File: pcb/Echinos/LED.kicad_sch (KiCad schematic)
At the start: 14 parts

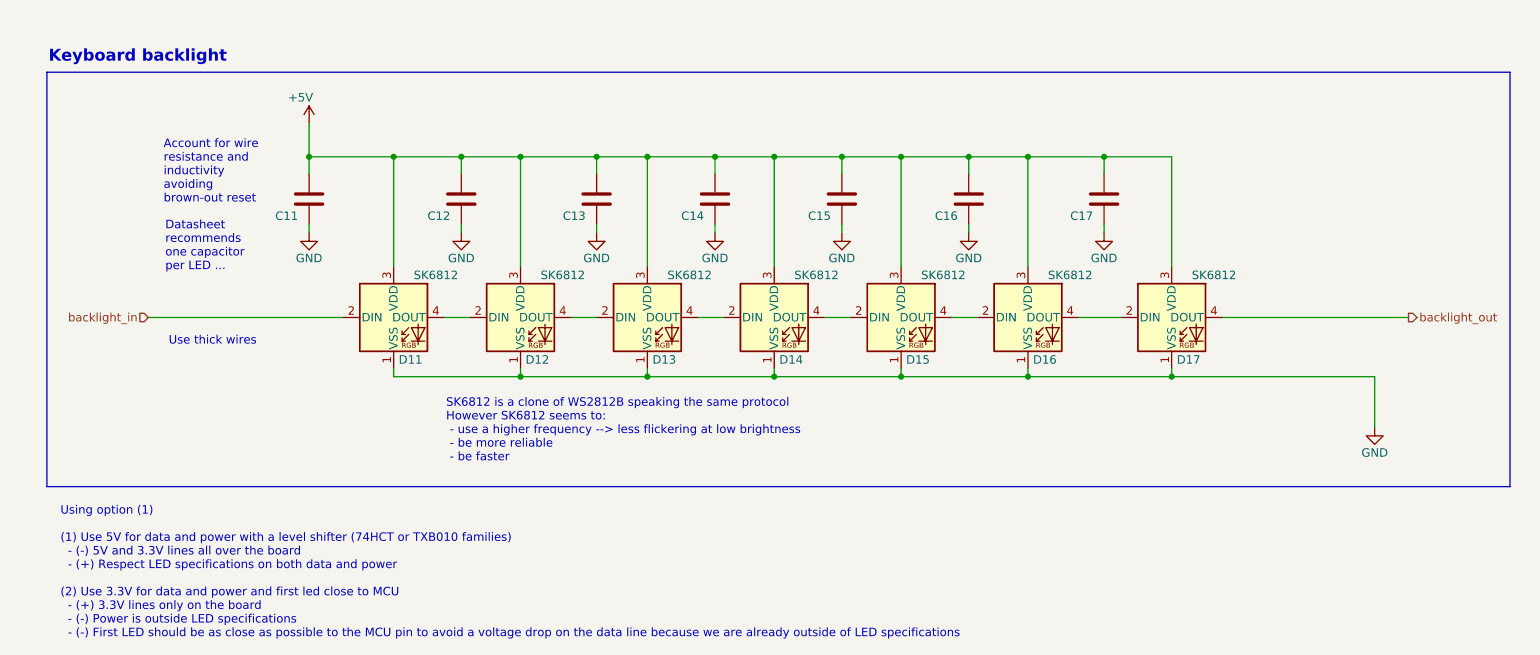
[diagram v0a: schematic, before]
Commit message: [PCB] - Save last state with on board RP2040.   - Create right side and route all components   - Component still on the bottom side to be able to merge both side for manufacturing
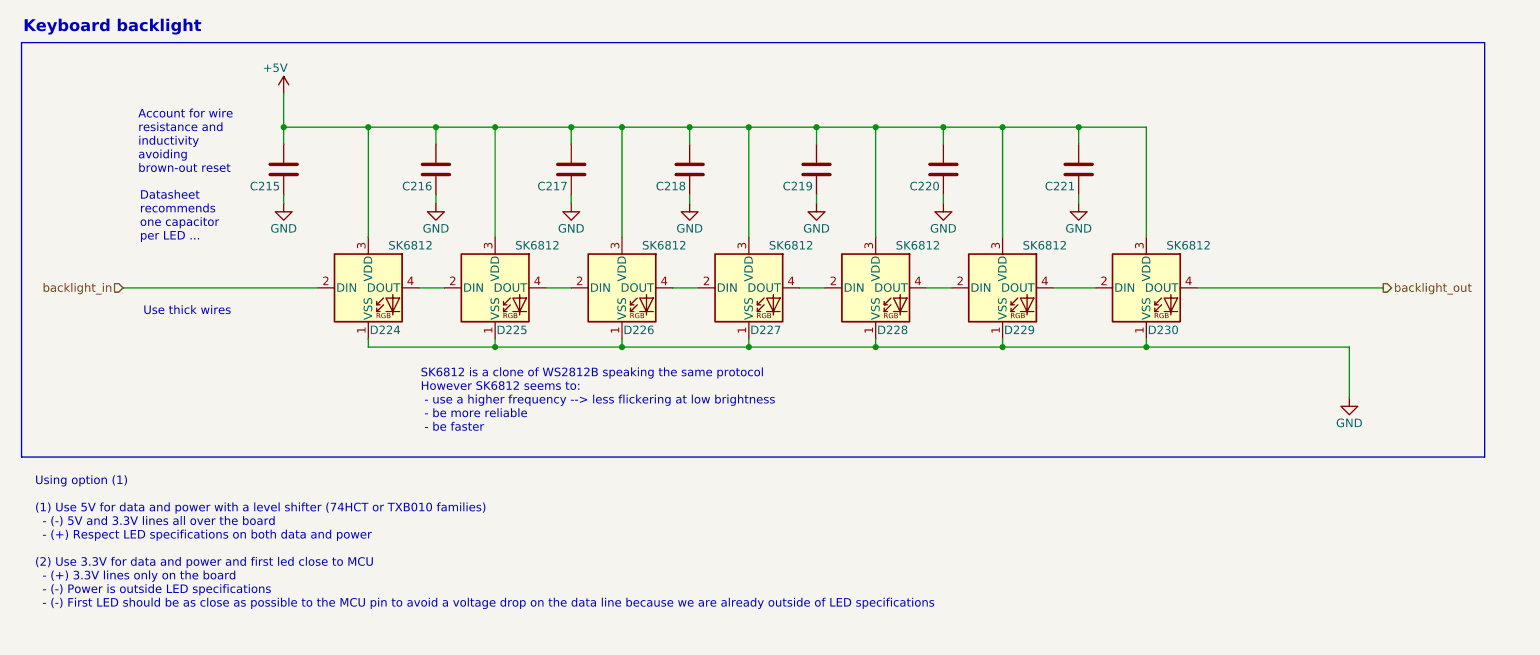
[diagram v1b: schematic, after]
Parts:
- renumbered C11 to C215, C12 to C216, C13 to C217, C14 to C218, C15 to C219, C16 to C220, C17 to C221, D11 to D224, D12 to D225, D13 to D226, D14 to D227, D15 to D228, D16 to D229, D17 to D230
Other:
- title: Backlight -> Backlight (Left)
- moved on the sheet: C215, C216, C217, C218, C219, C220, C221, D224, D225, D226, D227, D228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

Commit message: [PCB] - Save last state with on board RP2040.   - Fix flash component orientation for JLCPCB assembly   - Add logo + version   - Add TH in flash footprint and use the same zone fill method as for RP2040 footprint   - Improve ground planes under switches (right side)   - Move unused schematics to backup folder (will be used to create keyboard modules later)   - Add manufacturer and part name (mfr)   - Mark optional parts as DNP   - Resync with official RP2040 symbol and update pins matching
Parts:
- C215, C216, C217, C218, C219, C220, C221: MFR (none) -> CL21B104KBCNNNC; Manufacturer (none) -> Samsung Electro-Mechanics
- D224, D225, D226, D227, D228, D229, D230: MFR (none) -> SK6812A; Manufacturer (none) -> OPSCO Optoelectronics

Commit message: 🚀 [PCB] - Board RP2040 sent in production.
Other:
- note added: "Baking required (msl = 5a) - SK6812A LEDs (C190862) --> parts D224 to D230"
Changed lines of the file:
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@@
+		)
+	)
+	(text "Baking required (msl = 5a)\n  - SK6812A LEDs (C190862) --> parts D224 to D230"
+		(exclude_from_sim no)
+		(at 148.59 69.215 0)
+		(effects
+			(font
+				(size 1.27 1.27)
+				(thickness 0.254)
+				(bold yes)
+			)
+			(justify left)
 		)
 	)
